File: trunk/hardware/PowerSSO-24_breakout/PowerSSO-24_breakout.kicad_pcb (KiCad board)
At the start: 2 copper layers, 39.4 x 19.1 mm, 26 parts, among them P101 CONN_1, P102 CONN_1, P103 CONN_1, P104 CONN_1, P105 CONN_1, P106 CONN_1, P107 CONN_2, P108 CONN_2, U101 VND5E025AKTR

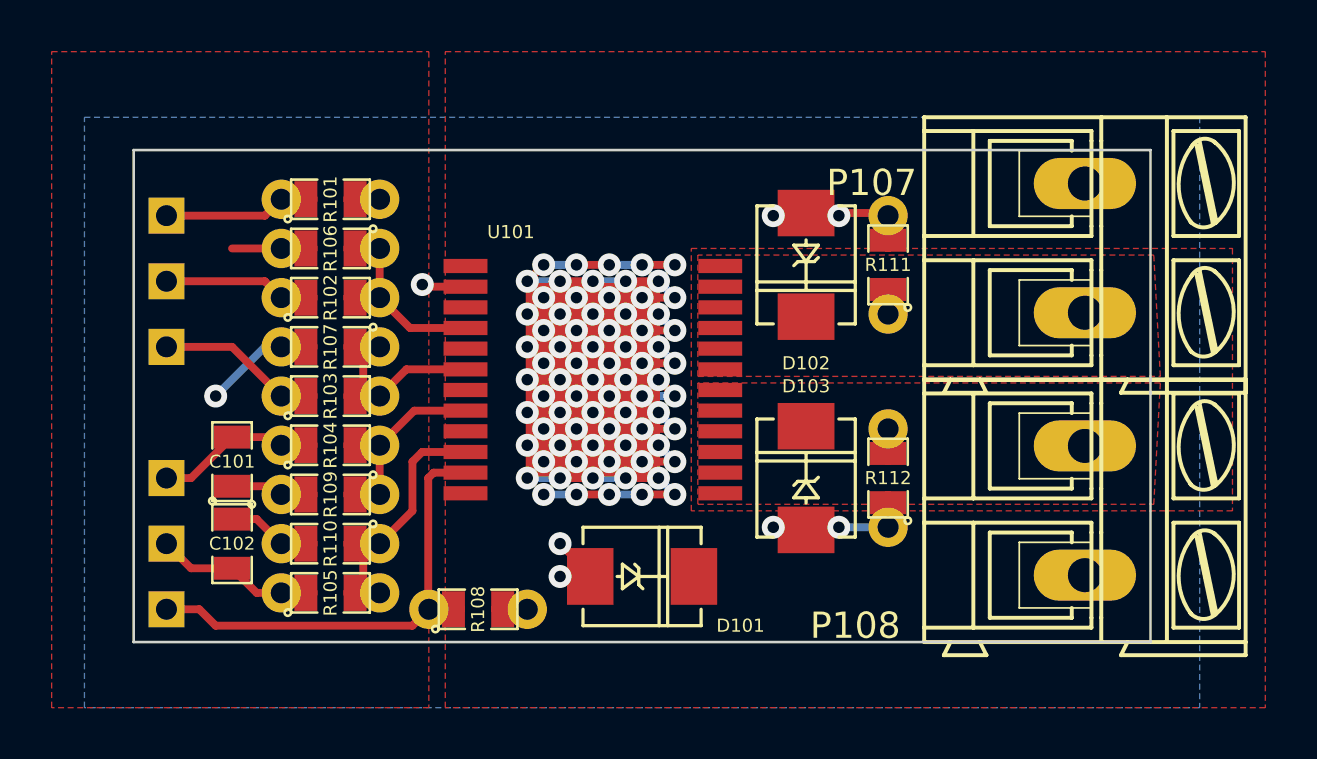
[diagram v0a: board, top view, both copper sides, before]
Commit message: 
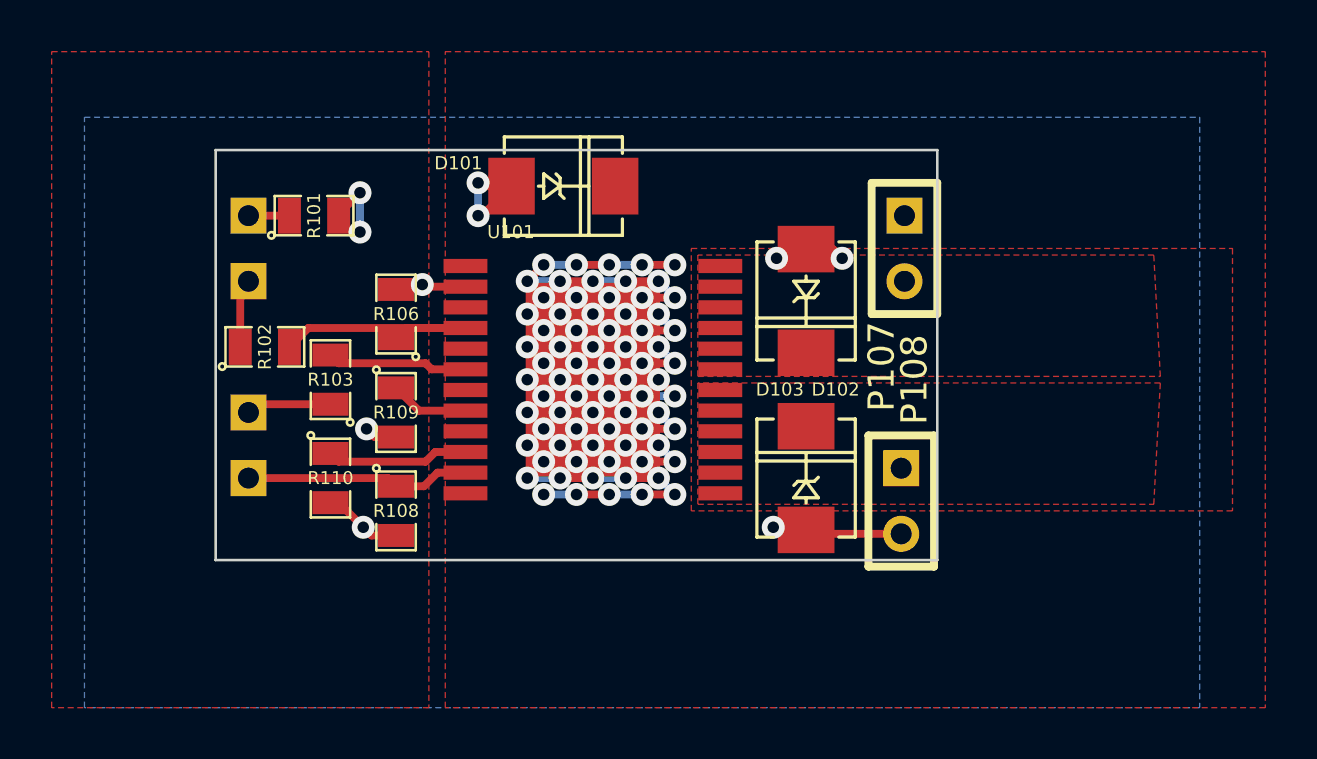
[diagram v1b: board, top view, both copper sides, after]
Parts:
- removed C101, C102: .01uF, SM0805
- removed P104, P105: CONN_1, SIL-1
- removed R104, R105, R107: 10K, SM0805_jumper
- removed R111, R112: 22K, SM0805_jumper
- P107, P108: footprint AK300-2 -> SIL-2
- R101, R102, R103, R106, R108: footprint SM0805_jumper -> SM0805
- R109, R110: value TBD -> 1K; footprint SM0805_jumper -> SM0805
- moved D101 15.4 mm to (229.4, 142.4)
- moved P108 7.12 mm to (242.4, 154.6)
- moved P107 6.99 mm to (242.6, 144.8)
- moved P106 5.99 mm to (217.2, 153.7)
- moved R108 4.96 mm to (222.9, 154.9), turned to 270 degrees
- moved R109 4.07 mm to (222.9, 151.1), turned to 270 degrees
- moved P103 4.07 mm to (217.2, 151.1)
- moved R106 3.59 mm to (222.9, 147.3), turned to 90 degrees
- moved R102 3.17 mm to (217.8, 148.6)
- moved P101 3.17 mm to (217.2, 143.5)
- moved P102 3.17 mm to (217.2, 146.1)
- moved R110 2.54 mm to (220.3, 153.7), turned to 270 degrees
- moved D102 1.40 mm to (238.8, 146.8)
- moved R101 0.90 mm to (219.7, 143.5)
- moved R103 0.63 mm to (220.3, 149.9), turned to 90 degrees
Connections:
- P107 pad 1: GND -> /VCC
- P108 pad 2: /VCC -> GND
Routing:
- net /CS_DIS: track 17.3 -> 8.75 mm
- net GND: track 27.1 -> 21.1 mm, vias 8 -> 10
- net N-000005: track 5.23 -> 0.00 mm
- net N-000001 (its old number): track 5.23 -> 0.00 mm
- net /IN2: track 5.71 -> 9.98 mm
- net /I1: track 7.05 -> 3.05 mm
- net N-000001: track 4.71 -> 1.59 mm
- net /I2: track 8.08 -> 5.51 mm
- net N-000004: track 4.71 -> 2.67 mm
- net N-000003: track 5.23 -> 3.31 mm
- net /IN1: track 6.55 -> 5.46 mm
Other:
- board size 39.4 x 19.1 mm -> 27.9 x 15.9 mm
- board text added: "CS"
- board text added: "GND"
- board text added: "IN1"
- board text added: "IN2"
- board text added: "VCC O2 O1 GND"
- board text removed: "GND O2 O1 VCC"

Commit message: 
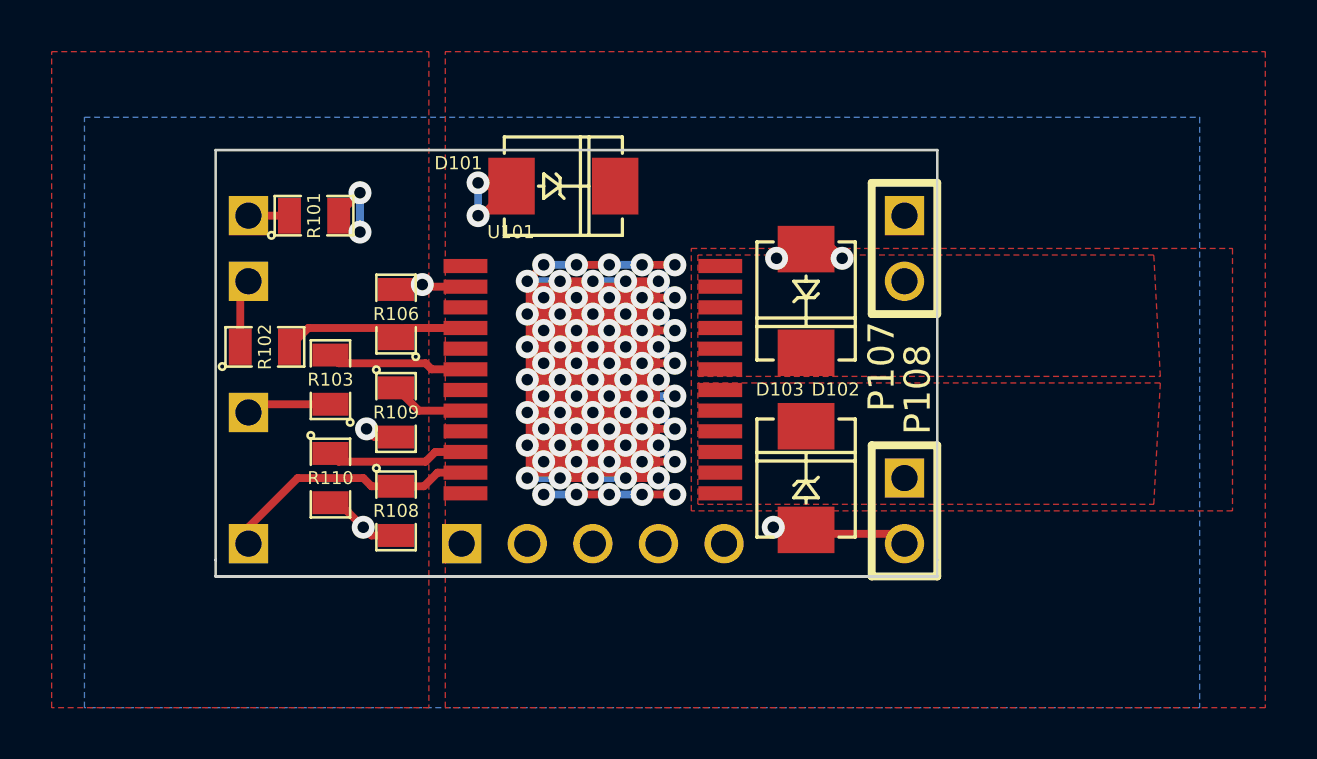
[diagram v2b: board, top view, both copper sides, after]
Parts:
- added P104: CONN_5, SIL-5, B.Cu at (231.8, 156.2)
- moved P106 2.54 mm to (217.2, 156.2)
- moved P108 0.40 mm to (242.6, 154.9)
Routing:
- net /CS_DIS: track 8.75 -> 10.2 mm
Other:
- board size 27.9 x 15.9 mm -> 27.9 x 16.5 mm
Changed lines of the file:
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@@
     (links 37)
     (no_connects 0)
-    (area 207.594287 137.16 256.540001 162.941423)
+    (area 206.959287 137.16 256.540001 162.941423)
     (thickness 1.6)
-    (drawings 12)
-    (tracks 207)
+    (drawings 15)
+    (tracks 210)
     (zones 0)
-    (modules 17)
+    (modules 18)
     (nets 13)
   )
@@
     (mod_text_size 1 1)
     (mod_text_width 0.15)
-    (pad_size 1.5 1.5)
-    (pad_drill 0.6)
+    (pad_size 1.524 1.524)
+    (pad_drill 1.016)
     (pad_to_mask_clearance 0)
     (aux_axis_origin 0 0)
@@
   (net 9 GND)
   (net 10 N-000001)
-  (net 11 N-000003)
-  (net 12 N-000004)
+  (net 11 N-000004)
+  (net 12 N-000005)
   (net_class Default "This is the default net class."
     (clearance 0.24892)
@@
     (add_net GND)
     (add_net N-000001)
-    (add_net N-000003)
     (add_net N-000004)
+    (add_net N-000005)
   )
   (net_class FAT ""
@@
     (fp_line (start -1.27 -1.27) (end -1.27 1.27) (layer B.SilkS) (width 0.3048))
     (fp_line (start 1.27 1.27) (end 1.27 -1.27) (layer B.SilkS) (width 0.3048))
-    (pad 1 thru_hole rect (at 0 0) (size 1.397 1.397) (drill 0.8128)
+    (pad 1 thru_hole rect (at 0 0) (size 1.524 1.524) (drill 1.016)
       (layers *.Cu *.Mask B.SilkS)
-      (net 11 N-000003)
+      (net 11 N-000004)
     )
   )
   (module SIL-1 (layer B.Cu)
-    (at 217.17 153.67)
+    (at 217.17 156.21)
     (descr "Connecteurs 1 pin")
     (tags "CONN DEV")
@@
     (fp_line (start -1.27 -1.27) (end -1.27 1.27) (layer B.SilkS) (width 0.3048))
     (fp_line (start 1.27 1.27) (end 1.27 -1.27) (layer B.SilkS) (width 0.3048))
-    (pad 1 thru_hole rect (at 0 0) (size 1.397 1.397) (drill 0.8128)
+    (pad 1 thru_hole rect (at 0 0) (size 1.524 1.524) (drill 1.016)
       (layers *.Cu *.Mask B.SilkS)
       (net 1 /CS_DIS)
@@
     (fp_line (start -1.27 -1.27) (end -1.27 1.27) (layer B.SilkS) (width 0.3048))
     (fp_line (start 1.27 1.27) (end 1.27 -1.27) (layer B.SilkS) (width 0.3048))
-    (pad 1 thru_hole rect (at 0 0) (size 1.397 1.397) (drill 0.8128)
+    (pad 1 thru_hole rect (at 0 0) (size 1.524 1.524) (drill 1.016)
       (layers *.Cu *.Mask B.SilkS)
       (net 10 N-000001)
@@
     (fp_line (start -1.27 -1.27) (end -1.27 1.27) (layer B.SilkS) (width 0.3048))
     (fp_line (start 1.27 1.27) (end 1.27 -1.27) (layer B.SilkS) (width 0.3048))
-    (pad 1 thru_hole rect (at 0 0) (size 1.397 1.397) (drill 0.8128)
+    (pad 1 thru_hole rect (at 0 0) (size 1.524 1.524) (drill 1.016)
       (layers *.Cu *.Mask B.SilkS)
-      (net 12 N-000004)
+      (net 12 N-000005)
     )
   )
@@
     (pad 1 smd rect (at -0.9525 0 90) (size 0.889 1.397)
       (layers F.Cu F.Paste F.Mask)
-      (net 11 N-000003)
+      (net 11 N-000004)
     )
     (pad 2 smd rect (at 0.9525 0 90) (size 0.889 1.397)
@@
     (pad 1 smd rect (at -0.9525 0) (size 0.889 1.397)
       (layers F.Cu F.Paste F.Mask)
-      (net 12 N-000004)
+      (net 12 N-000005)
     )
     (pad 2 smd rect (at 0.9525 0) (size 0.889 1.397)
@@
   )
   (module SIL-2 (layer F.Cu)
-    (at 242.443 154.559 270)
+    (at 242.57 154.94 270)
     (descr "Connecteurs 2 pins")
     (tags "CONN DEV")
@@
     (fp_line (start 2.54 -1.27) (end 2.54 1.27) (layer F.SilkS) (width 0.3048))
     (fp_line (start 2.54 1.27) (end -2.54 1.27) (layer F.SilkS) (width 0.3048))
-    (pad 1 thru_hole rect (at -1.27 0 270) (size 1.397 1.397) (drill 0.8128)
+    (pad 1 thru_hole rect (at -1.27 0 270) (size 1.524 1.524) (drill 1.016)
       (layers *.Cu *.Mask F.SilkS)
       (net 6 /O1)
     )
-    (pad 2 thru_hole circle (at 1.27 0 270) (size 1.397 1.397) (drill 0.8128)
+    (pad 2 thru_hole circle (at 1.27 0 270) (size 1.524 1.524) (drill 1.016)
       (layers *.Cu *.Mask F.SilkS)
       (net 9 GND)
@@
     (fp_line (start 2.54 -1.27) (end 2.54 1.27) (layer F.SilkS) (width 0.3048))
     (fp_line (start 2.54 1.27) (end -2.54 1.27) (layer F.SilkS) (width 0.3048))
-    (pad 1 thru_hole rect (at -1.27 0 270) (size 1.397 1.397) (drill 0.8128)
+    (pad 1 thru_hole rect (at -1.27 0 270) (size 1.524 1.524) (drill 1.016)
       (layers *.Cu *.Mask F.SilkS)
       (net 8 /VCC)
     )
-    (pad 2 thru_hole circle (at 1.27 0 270) (size 1.397 1.397) (drill 0.8128)
+    (pad 2 thru_hole circle (at 1.27 0 270) (size 1.524 1.524) (drill 1.016)
       (layers *.Cu *.Mask F.SilkS)
       (net 7 /O2)
     )
   )
+  (module SIL-5 (layer B.Cu)
+    (at 231.775 156.21)
+    (descr "Connecteur 5 pins")
+    (tags "CONN DEV")
+    (fp_text reference P104 (at -6.35 -1.905) (layer B.SilkS)
+      (effects (font (size 0.762 0.762) (thickness 0.1905)) (justify mirror))
+    )
+    (fp_text value CONN_5 (at 0 2.54) (layer B.SilkS) hide
+      (effects (font (size 1.524 1.016) (thickness 0.3048)) (justify mirror))
+    )
+    (fp_line (start -7.62 -1.27) (end -7.62 1.27) (layer B.SilkS) (width 0.3048))
+    (fp_line (start -7.62 1.27) (end 5.08 1.27) (layer B.SilkS) (width 0.3048))
+    (fp_line (start 5.08 1.27) (end 5.08 -1.27) (layer B.SilkS) (width 0.3048))
+    (fp_line (start 5.08 -1.27) (end -7.62 -1.27) (layer B.SilkS) (width 0.3048))
+    (fp_line (start -5.08 -1.27) (end -5.08 1.27) (layer B.SilkS) (width 0.3048))
+    (pad 1 thru_hole rect (at -6.35 0) (size 1.524 1.524) (drill 1.016)
+      (layers *.Cu *.Mask B.SilkS)
+    )
+    (pad 2 thru_hole circle (at -3.81 0) (size 1.524 1.524) (drill 1.016)
+      (layers *.Cu *.Mask B.SilkS)
+    )
+    (pad 3 thru_hole circle (at -1.27 0) (size 1.524 1.524) (drill 1.016)
+      (layers *.Cu *.Mask B.SilkS)
+    )
+    (pad 4 thru_hole circle (at 1.27 0) (size 1.524 1.524) (drill 1.016)
+      (layers *.Cu *.Mask B.SilkS)
+    )
+    (pad 5 thru_hole circle (at 3.81 0) (size 1.524 1.524) (drill 1.016)
+      (layers *.Cu *.Mask B.SilkS)
+    )
+  )
+  (dimension 16.51 (width 0.3) (layer Dwgs.User)
+    (gr_text "0.6500 in" (at 212.645 149.225 90) (layer Dwgs.User)
+      (effects (font (size 1.5 1.5) (thickness 0.3)))
+    )
+    (feature1 (pts (xy 215.265 140.97) (xy 211.295 140.97)))
+    (feature2 (pts (xy 215.265 157.48) (xy 211.295 157.48)))
+    (crossbar (pts (xy 213.995 157.48) (xy 213.995 140.97)))
+    (arrow1a (pts (xy 213.995 140.97) (xy 214.58142 142.096503)))
+    (arrow1b (pts (xy 213.995 140.97) (xy 213.40858 142.096503)))
+    (arrow2a (pts (xy 213.995 157.48) (xy 214.58142 156.353497)))
+    (arrow2b (pts (xy 213.995 157.48) (xy 213.40858 156.353497)))
+  )
+  (gr_line (start 215.9 156.845) (end 215.9 157.48) (angle 90) (layer Edge.Cuts) (width 0.1))
+  (gr_line (start 243.84 157.48) (end 215.9 157.48) (angle 90) (layer Edge.Cuts) (width 0.1))
+  (gr_line (start 243.84 156.845) (end 243.84 157.48) (angle 90) (layer Edge.Cuts) (width 0.1))
   (gr_text CS (at 219.456 154.813) (layer B.SilkS)
     (effects (font (size 0.762 0.762) (thickness 0.127)) (justify mirror))
@@
   (gr_text IN2 (at 219.583 147.066) (layer B.SilkS)
     (effects (font (size 0.762 0.762) (thickness 0.127)) (justify mirror))
-  )
-  (dimension 15.875 (width 0.3) (layer Dwgs.User)
-    (gr_text "0.6250 in" (at 213.28 148.9075 90) (layer Dwgs.User)
-      (effects (font (size 1.5 1.5) (thickness 0.3)))
-    )
-    (feature1 (pts (xy 215.265 140.97) (xy 211.93 140.97)))
-    (feature2 (pts (xy 215.265 156.845) (xy 211.93 156.845)))
-    (crossbar (pts (xy 214.63 156.845) (xy 214.63 140.97)))
-    (arrow1a (pts (xy 214.63 140.97) (xy 215.21642 142.096503)))
-    (arrow1b (pts (xy 214.63 140.97) (xy 214.04358 142.096503)))
-    (arrow2a (pts (xy 214.63 156.845) (xy 215.21642 155.718497)))
-    (arrow2b (pts (xy 214.63 156.845) (xy 214.04358 155.718497)))
   )
   (dimension 27.94 (width 0.3) (layer Dwgs.User)
@@
   (gr_line (start 215.9 156.845) (end 215.9 140.97) (angle 90) (layer Edge.Cuts) (width 0.1))
   (gr_line (start 215.9 140.97) (end 243.84 140.97) (angle 90) (layer Edge.Cuts) (width 0.1))
-  (gr_line (start 215.9 156.845) (end 243.84 156.845) (angle 90) (layer Edge.Cuts) (width 0.1))
+  (gr_line (start 215.9 157.48) (end 243.84 157.48) (angle 90) (layer Edge.Cuts) (width 0.1))
   (gr_text "R0.1\nAlt_breakout" (at 231.14 142.24) (layer B.SilkS)
     (effects (font (size 1.016 1.016) (thickness 0.127)) (justify mirror))
@@
     (effects (font (size 1.016 1.016) (thickness 0.2032)) (justify mirror))
   )
+  (segment (start 222.885 153.9875) (end 221.9325 153.9875) (width 0.3048) (layer F.Cu) (net 1))
+  (segment (start 217.17 155.575) (end 217.17 156.21) (width 0.3048) (layer F.Cu) (net 1))
+  (segment (start 219.075 153.67) (end 217.17 155.575) (width 0.3048) (layer F.Cu) (net 1))
+  (segment (start 221.615 153.67) (end 219.075 153.67) (width 0.3048) (layer F.Cu) (net 1))
+  (segment (start 221.9325 153.9875) (end 221.615 153.67) (width 0.3048) (layer F.Cu) (net 1))
   (segment (start 225.5725 153.46) (end 224.492 153.46) (width 0.3048) (layer F.Cu) (net 1))
   (segment (start 223.9645 153.9875) (end 222.885 153.9875) (width 0.3048) (layer F.Cu) (net 1))
   (segment (start 224.492 153.46) (end 223.9645 153.9875) (width 0.3048) (layer F.Cu) (net 1))
-  (segment (start 217.17 153.67) (end 222.5675 153.67) (width 0.3048) (layer F.Cu) (net 1))
-  (segment (start 222.5675 153.67) (end 222.885 153.9875) (width 0.3048) (layer F.Cu) (net 1))
   (segment (start 225.5725 151.06) (end 223.7675 151.06) (width 0.3048) (layer F.Cu) (net 2))
   (segment (start 223.7675 151.06) (end 222.885 150.1775) (width 0.3048) (layer F.Cu) (net 2))
